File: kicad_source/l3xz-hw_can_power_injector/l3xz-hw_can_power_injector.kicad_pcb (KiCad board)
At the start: 2 copper layers, 46 x 51 mm, 42 parts, among them CN1 Conn_01x02, CN2 Conn_01x04, CN3 Conn_01x04, CN4 Conn_01x02, CN5 Conn_01x04, CN6 Conn_01x04, CN7 Conn_01x02, U1 RAA211650

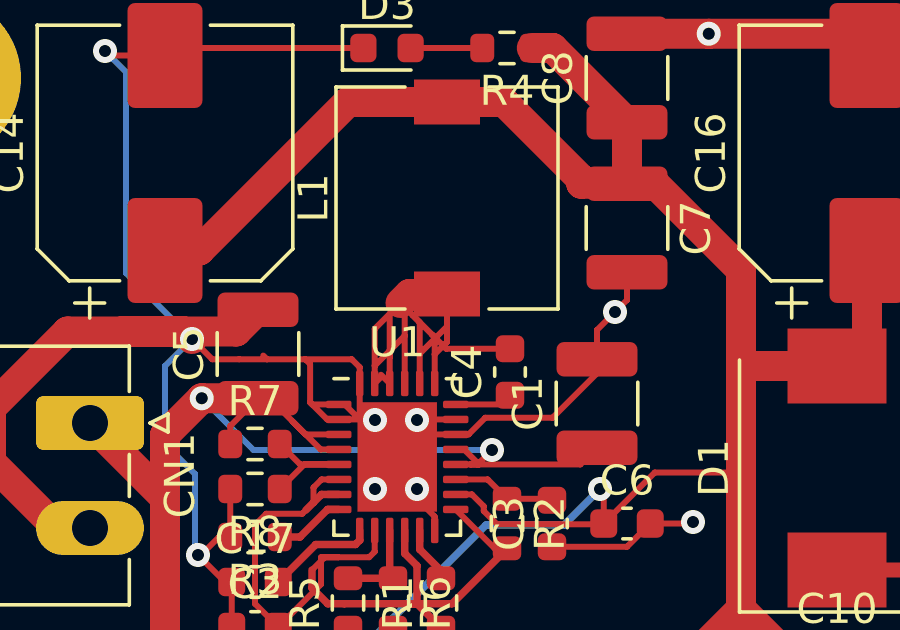
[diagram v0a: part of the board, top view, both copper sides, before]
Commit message: updated some component values
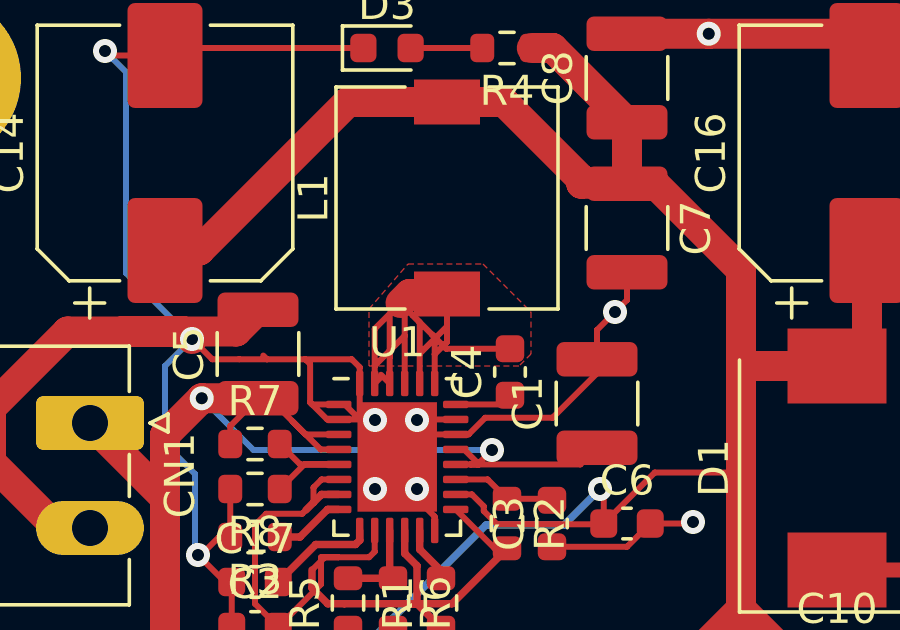
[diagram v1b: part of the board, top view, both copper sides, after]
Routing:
- added copper zone on F.Cu, net /PHASE
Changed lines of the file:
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@@
   (segment (start 107.106174 102.881174) (end 106.425 102.2) (width 0.2) (layer "F.Cu") (net 23))
   (segment (start 108.39 102.881174) (end 107.106174 102.881174) (width 0.2) (layer "F.Cu") (net 23))
+  (zone (net 7) (net_name "/PHASE") (layer "F.Cu") (hatch edge 0.508)
+    (priority 1)
+    (connect_pads (clearance 0.2))
+    (min_thickness 0.2) (filled_areas_thickness no)
+    (fill yes (thermal_gap 0.2) (thermal_bridge_width 0.2))
+    (polygon
+      (pts
+        (xy 114.8 97.8)
+        (xy 114.8 99.2)
+        (xy 114.4 99.6)
+        (xy 109.4 99.6)
+        (xy 109.4 97.7)
+        (xy 110.7 96.2)
+        (xy 113.2 96.2)
+      )
+    )
+  )
   (zone (net 2) (net_name "GND") (layer "F.Cu") (hatch edge 0.508)
     (connect_pads (clearance 0.508))

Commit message: made drc, corrected some errors, added label
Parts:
- added L2: Label, generationmake:generationmake_small_silk, B.Cu at (115.1, 119.6)
- added L3: Label, generationmake:generationmake_small_solder, F.Cu at (117.0, 126.2)
- C1, C5: value C_Small -> 4.7uF 50V
- C10, C7, C8: value C_Small -> 47uF 10V
- C11, C9: value C_Small -> 100nF
- C12, C13, C15: value 100 uF / 50 V -> 220 uF / 50 V
- C14, C16: value 470 uF / 10 V -> 1000 uF / 10 V
- CN1, CN7: value Conn_01x02 -> DNI
- CN2, CN3, CN5, CN6: value Conn_01x04 -> SM04B-GHS-TB; footprint Connector_JST:JST_GH_BM04B-GHS-TBT_1x04-1MP_P1.25mm_Vertical -> Connector_JST:JST_GH_SM04B-GHS-TB_1x04-1MP_P1.25mm_Horizontal
- L1: footprint Inductor_SMD:L_7.3x7.3_H4.5 -> Inductor_SMD:L_Wuerth_HCI-1050
- moved R4 18.9 mm to (96.3, 95.5)
- moved D3 15.9 mm to (96.3, 97.1), turned to 180 degrees
- moved C7 1.73 mm to (119.7, 94.7)
- moved C8 1.70 mm to (119.7, 90.0)
- moved L1 1.06 mm to (112.7, 93.2)
- moved C4 0.91 mm to (114.2, 100.7)
- moved C1 0.46 mm to (117.3, 101.2), turned to 0 degrees
- moved C17 0.10 mm to (105.6, 106.9)
- moved C2 0.10 mm to (105.6, 108.4)
- moved R3 0.10 mm to (105.6, 105.4)
- moved R7 0.10 mm to (105.6, 102.3)
- moved R8 0.10 mm to (105.6, 103.8)
- turned CN2 to 90 degrees
- turned CN3 to 90 degrees
- turned CN5 to 90 degrees
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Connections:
- CN2 pad MP: (no net) -> /MP
- CN3 pad MP: (no net) -> /MP
- CN5 pad MP: (no net) -> /MP
- CN6 pad MP: (no net) -> /MP
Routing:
- net /MP: track 0.00 -> 49.5 mm, vias 0 -> 16
- net VCC: track 82.8 -> 97.4 mm
- net GND: track 150.5 -> 136.3 mm, vias 17 -> 27
- net /PHASE: track 25.5 -> 26.4 mm
- net Net-(D3-Pad2): track 2.39 -> 1.62 mm
- net /CAN1VCC: track 22.3 -> 23.0 mm
- net /CAN1H: track 13.4 -> 12.8 mm

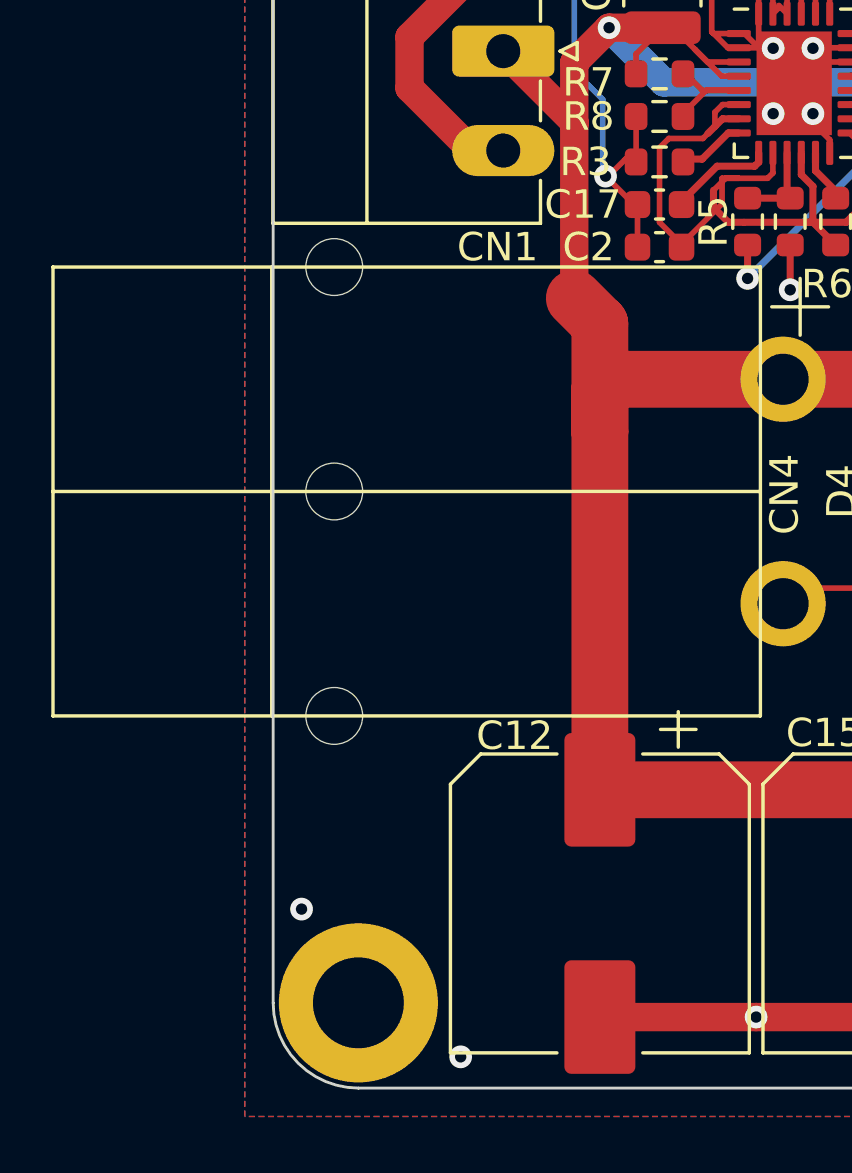
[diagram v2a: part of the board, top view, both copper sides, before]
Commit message: added some texts to pcb, generated BOM, updated schemtatic pdf
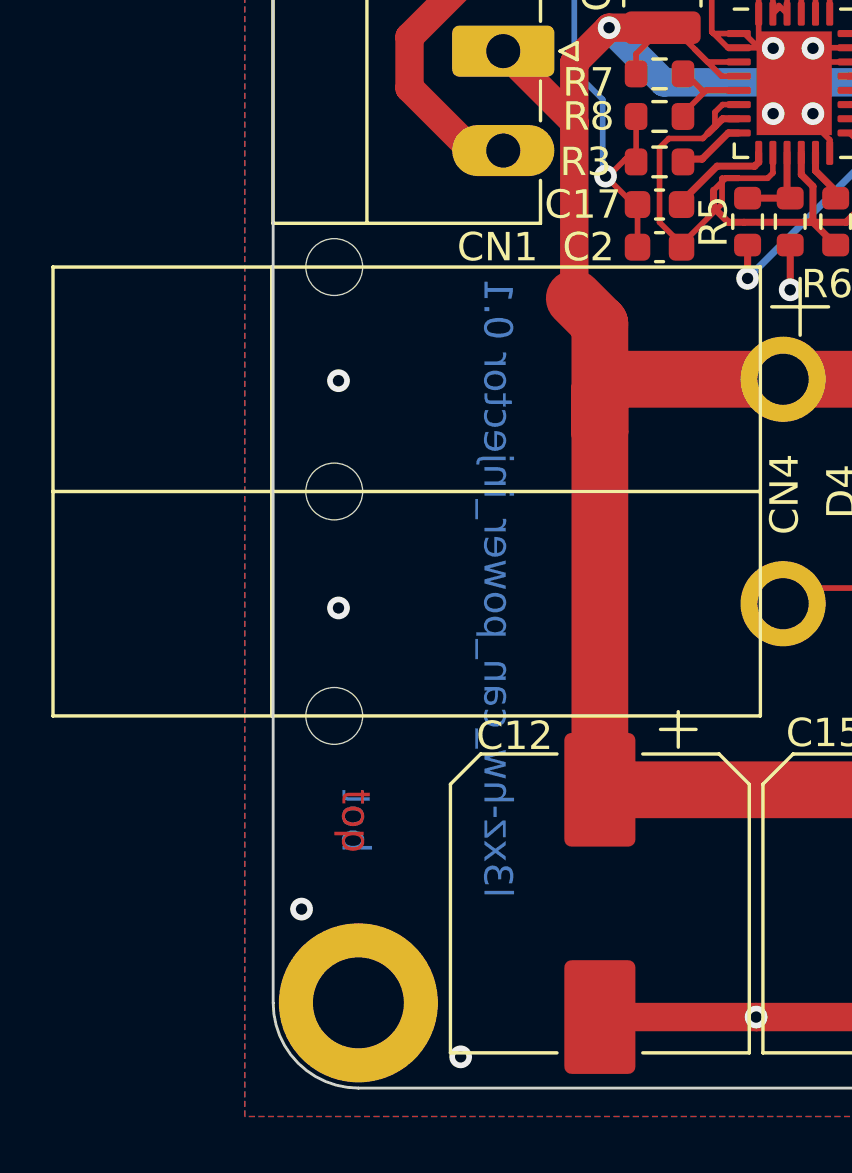
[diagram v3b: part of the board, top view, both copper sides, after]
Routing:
- net GND: vias 27 -> 29
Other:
- board text added: "bot"
- board text added: "l3xz-hw_can_power_injector 0.1"
- board text added: "top"
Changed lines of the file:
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@@
   (gr_arc (start 92 90) (mid 92.87868 87.87868) (end 95 87) (layer "Edge.Cuts") (width 0.1))
   (gr_line (start 138 135) (end 138 90) (layer "Edge.Cuts") (width 0.1))
+  (gr_text "top" (at 94.9 128.6 270) (layer "F.Cu")
+    (effects (font (size 1 1) (thickness 0.25)))
+  )
+  (gr_text "l3xz-hw_can_power_injector 0.1" (at 99.9 120.4 270) (layer "B.Cu")
+    (effects (font (size 1 1) (thickness 0.25)) (justify mirror))
+  )
+  (gr_text "bot" (at 94.9 128.6 270) (layer "B.Cu")
+    (effects (font (size 1 1) (thickness 0.25)) (justify mirror))
+  )
   (dimension (type aligned) (layer "Cmts.User")
     (pts (xy 95 87) (xy 95 138))
@@
   (via (at 111 103.7) (size 0.8) (drill 0.4) (layers "F.Cu" "B.Cu") (net 2))
   (via (at 134.6 105.6) (size 0.8) (drill 0.4) (layers "F.Cu" "B.Cu") (net 2))
+  (via (at 94.3 113.1) (size 0.8) (drill 0.4) (layers "F.Cu" "B.Cu") (free) (net 2))
   (via (at 109.4 88) (size 0.8) (drill 0.4) (layers "F.Cu" "B.Cu") (free) (net 2))
   (via (at 131.7 88) (size 0.8) (drill 0.4) (layers "F.Cu" "B.Cu") (free) (net 2))
@@
   (via (at 120.5 135.5) (size 0.8) (drill 0.4) (layers "F.Cu" "B.Cu") (net 2))
   (via (at 93 131.7) (size 0.8) (drill 0.4) (layers "F.Cu" "B.Cu") (free) (net 2))
+  (via (at 94.3 121.1) (size 0.8) (drill 0.4) (layers "F.Cu" "B.Cu") (free) (net 2))
   (via (at 131.5 136.9) (size 0.8) (drill 0.4) (layers "F.Cu" "B.Cu") (free) (net 2))
   (via (at 134.5 124.6) (size 0.8) (drill 0.4) (layers "F.Cu" "B.Cu") (net 2))

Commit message: added some labels
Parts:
- added L4: Label, generationmake:opencyphal_small, B.Cu at (107.1, 94.0)
- C11, C9: value 100nF -> 100 nF
- CN4: value Conn_01x02 -> Powerpole_2
- D3: value LED_Small -> LED green
- L1: value 10 uH -> 7443251000 (10 uH)
- L2: footprint generationmake:generationmake_small_silk -> generationmake:generationmake_logo
- moved L2 2.70 mm to (114.6, 122.3)
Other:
- board text added: "+"
- board text added: "UCANPHY Micro ch. 1"
- board text added: "UCANPHY Micro ch. 2"
- board text added: "input voltage: 7 - 40 V"
- board text added: "prvides up to 5 A to the Cyphal network in total"
